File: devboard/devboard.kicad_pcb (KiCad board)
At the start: 2 copper layers, 139.7 x 50.5 mm, 6 parts, among them J1 IC1F-68RD-1.27SF(52), J2 92140-010LF, J3 DATA, J4 ADDR, J6 CE, J7 GND

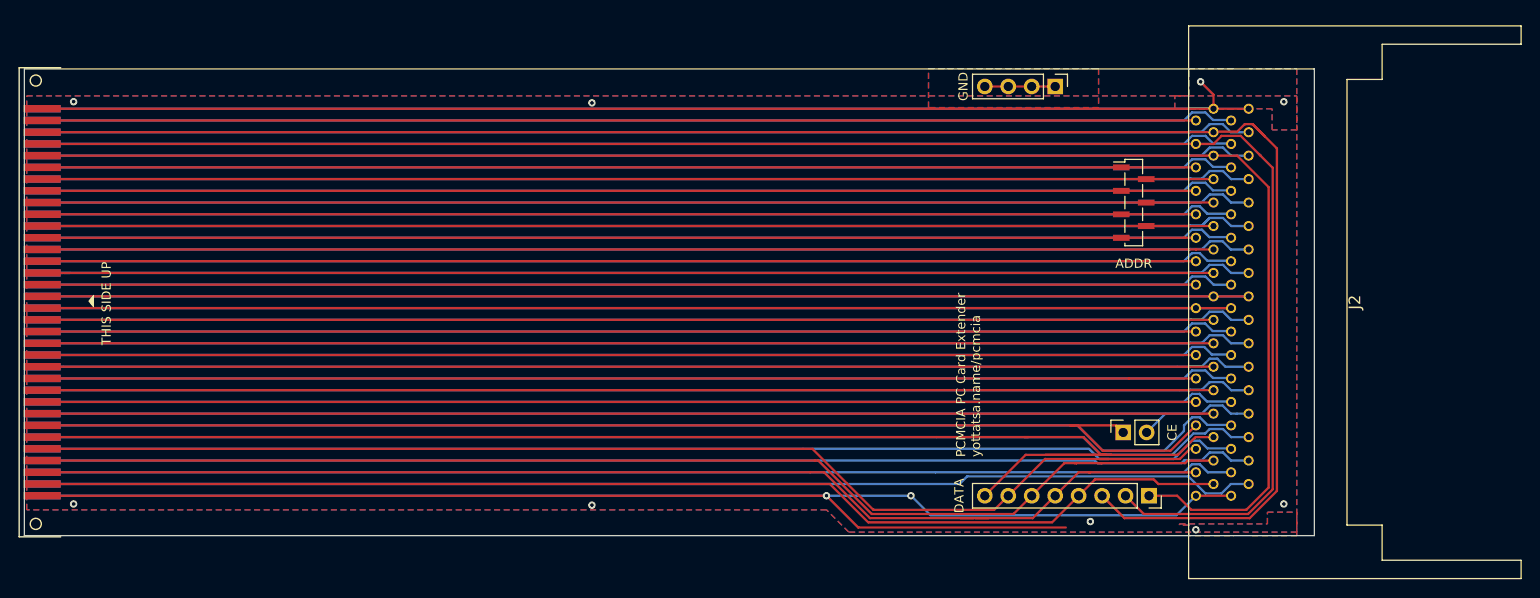
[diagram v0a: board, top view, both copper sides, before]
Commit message: new devboard
Adding 4 x 40 lines 0.5mm FPC ribbon connectors, 16 probing lines each.
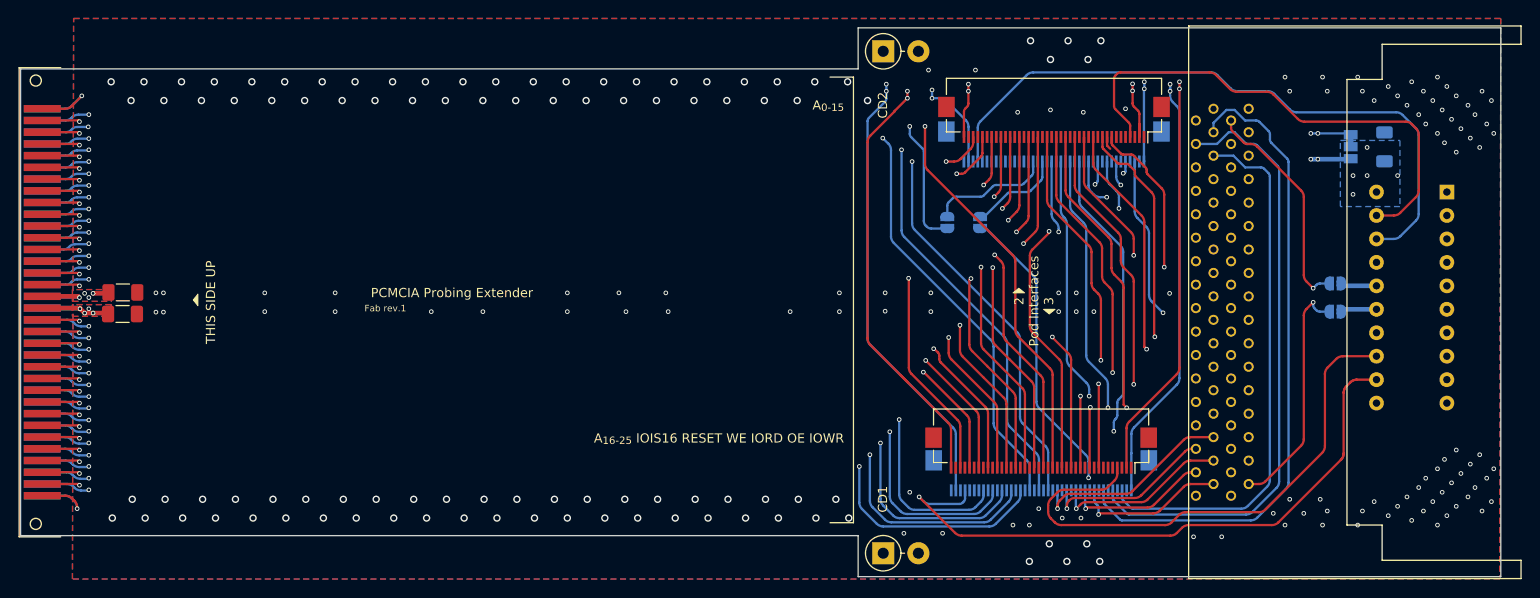
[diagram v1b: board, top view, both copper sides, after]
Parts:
- added C1: 1uF PWR, Capacitor_SMD:C_1206_3216Metric_Pad1.33x1.80mm_HandSolder, F.Cu at (88.0, 84.6)
- added C2: 1uF PWR, Capacitor_SMD:C_1206_3216Metric_Pad1.33x1.80mm_HandSolder, F.Cu at (88.0, 82.2)
- added C3: 1uF PWR, Capacitor_SMD:C_1206_3216Metric_Pad1.33x1.80mm_HandSolder, B.Cu at (224.6, 66.5)
- added J5: A_{16-25} IOIS16 RESET WE IORD OE IOWR, Connector_FFC-FPC:Hirose_FH12-40S-0.5SH_1x40-1MP_P0.50mm_Horizontal, F.Cu at (187.5, 99.4)
- added JP1: AUX PWR, Jumper:SolderJumper-3_P1.3mm_Bridged12_Pad1.0x1.5mm, B.Cu at (221.0, 66.5)
- added JP2: CD1, Jumper:SolderJumper-2_P1.3mm_Open_RoundedPad1.0x1.5mm, B.Cu at (219.3, 81.3)
- added JP3: CD2, Jumper:SolderJumper-2_P1.3mm_Open_RoundedPad1.0x1.5mm, B.Cu at (219.3, 84.3)
- added JP4: CD1, Jumper:SolderJumper-2_P1.3mm_Open_RoundedPad1.0x1.5mm, B.Cu at (180.8, 74.7)
- added JP5: CD2, Jumper:SolderJumper-2_P1.3mm_Open_RoundedPad1.0x1.5mm, B.Cu at (177.3, 74.7)
- added SW1: CD1, Diode_THT:D_DO-15_P3.81mm_Vertical_AnodeUp, F.Cu at (170.4, 110.5)
- added SW2: CD2, Diode_THT:D_DO-15_P3.81mm_Vertical_AnodeUp, F.Cu at (170.4, 56.1)
- J3: value DATA -> D_{0-15}; footprint Connector_PinSocket_2.54mm:PinSocket_1x08_P2.54mm_Vertical -> Connector_FFC-FPC:Hirose_FH12-40S-0.5SH_1x40-1MP_P0.50mm_Horizontal; moved to B.Cu
- J4: value ADDR -> A_{0-15}; footprint Connector_PinSocket_1.27mm:PinSocket_1x07_P1.27mm_Vertical_SMD_Pin1Left -> Connector_FFC-FPC:Hirose_FH12-40S-0.5SH_1x40-1MP_P0.50mm_Horizontal
- J6: value CE -> IREQ STSHG SPKR WAIT REG CE_{1,2} VS_{1,2} CD_{1,2} AUX_{1,4}; footprint Connector_PinSocket_2.54mm:PinSocket_1x02_P2.54mm_Vertical -> Connector_FFC-FPC:Hirose_FH12-40S-0.5SH_1x40-1MP_P0.50mm_Horizontal; moved to B.Cu
- J7: value GND -> REG RESET IREQ IOWR IORD OE CE_{1,2}; footprint Connector_PinHeader_2.54mm:PinHeader_1x04_P2.54mm_Vertical -> Package_DIP:DIP-20_W7.62mm; moved to B.Cu
- moved J7 43.9 mm to (231.4, 71.4), turned to 180 degrees
- moved J6 32.1 mm to (188.8, 66.2), turned to 0 degrees
- moved J4 12.4 mm to (188.8, 63.6), turned to 180 degrees
- moved J3 11.9 mm to (187.5, 101.8), turned to 0 degrees
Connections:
- net /VCC renamed 5V
- J1 pad 36: /CD1 -> /I.CD1
- J1 pad 67: /CD2 -> /I.CD2
- J3 pad 1: /D0 -> GND
- J3 pad 2: /D1 -> PROBE.5V
- J3 pad 3: /D2 -> GND
- J3 pad 4: /D3 -> /CLK1
- J3 pad 5: /D4 -> GND
- J3 pad 6: /D5 -> unconnected-(J3-Pin_6-Pad6)
- J3 pad 7: /D6 -> GND
- J3 pad 8: /D7 -> /D15
- J4 pad 1: /A0 -> GND
- J4 pad 2: /A1 -> PROBE.5V
- J4 pad 3: /A2 -> GND
- J4 pad 4: /A3 -> /CLK2
- J4 pad 5: /A4 -> GND
- J4 pad 6: /A5 -> unconnected-(J4-Pin_6-Pad6)
- J4 pad 7: /A6 -> GND
- J6 pad 1: /CE1 -> GND
- J6 pad 2: /CE2 -> PROBE.5V
- J7 pad 1: GND -> unconnected-(J7-I1/CLK-Pad1)
- J7 pad 2: GND -> /REG
- J7 pad 3: GND -> /RESET
- J7 pad 4: GND -> /IREQ
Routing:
- net GND: track 511.6 -> 27.8 mm, vias 10 -> 210
- net PROBE.5V: track 0.00 -> 244.7 mm, vias 0 -> 18
- net /VPP: track 261.3 -> 137.4 mm, vias 0 -> 4
- net /I.CD1: track 0.00 -> 96.8 mm, vias 0 -> 1
- net /I.CD2: track 0.00 -> 95.3 mm, vias 0 -> 1
- net 5V: track 257.5 -> 164.3 mm, vias 0 -> 6
- net /CLK4: track 0.00 -> 71.2 mm
- net /CLK1: track 0.00 -> 68.7 mm, vias 0 -> 1
- net /CE1: track 133.0 -> 193.8 mm, vias 0 -> 2
- net /CLK3: track 0.00 -> 59.2 mm
- net /CLK2: track 0.00 -> 55.0 mm
- net /CE2: track 134.3 -> 188.5 mm, vias 0 -> 2
- net /RESET: track 132.4 -> 183.1 mm, vias 0 -> 2
- net /IOWR: track 129.5 -> 177.2 mm, vias 0 -> 2
- net /CD2: track 129.5 -> 82.0 mm, vias 0 -> 2
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- added copper zone on B.Cu, net /VPP
- added copper zone on F.Cu, net /VPP
- added copper zone on In2.Cu, net /VPP
- added copper zone on B.Cu, net 5V
- added copper zone on F.Cu, net 5V
- added copper zone on In1.Cu, net 5V
- added copper zone on In1.Cu, net GND
- added copper zone on In2.Cu, net GND
- added copper zone on In1.Cu, net PROBE.5V
- added copper zone on B.Cu, net VAUX
- added copper zone on In1.Cu, net VAUX
- added copper zone on In2.Cu, net VAUX
- removed copper zone on B.Cu, net /GND
- removed copper zone on F.Cu, net /GND
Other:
- board size 139.7 x 50.5 mm -> 160.3 x 59.4 mm
- copper layers 2 -> 4
- net class Default removed
- board text added: "0.5mm FPC ribbon pinout Pins 2 and 40 is +5V probe power Pin 4 is the clock Even pins from 38 to 8 are data pins Odd pins starting from 1 is GND"
- board text added: "2 Pod Interfaces 3"
- board text added: "4 Pod Interfaces 1"
- board text added: "CLK2 CLK4 CLK3 CLK1"
- board text added: "Fab rev.1"
- board text added: "PCMCIA Probing Extender"
- board text added: "REG RESET IREQ IOWR IORD OE CE_{1} CE_{2}"
- board text removed: "PCMCIA PC Card Extender yottatsa.name/pcmcia"

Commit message: devboard test
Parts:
- JP2: value CD1 -> CD2
- JP3: value CD2 -> CD1
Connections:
- J7 pad 12: /CLK1 -> /CLK4
- J7 pad 13: /CLK3 -> /CLK1
- J7 pad 18: /CLK4 -> /CLK3
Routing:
- net /CLK4: track 71.2 -> 87.4 mm
- net /CLK3: track 59.2 -> 70.5 mm
- net /D3: track 143.7 -> 132.7 mm
- net /CLK1: track 68.7 -> 69.8 mm
- net GND: vias 210 -> 213
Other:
- board text added: "1 Pod Interfaces 2"
- board text added: "4 Pod Interfaces 3"
- board text added: "Clock 1 J Clock 2 K Clock 3 L Clock 4 M"
- board text added: "Fab rev.2"
- board text added: "J K L M"
- board text removed: "2 Pod Interfaces 3"
- board text removed: "4 Pod Interfaces 1"
- board text removed: "CLK2 CLK4 CLK3 CLK1"
- board text removed: "Fab rev.1"
